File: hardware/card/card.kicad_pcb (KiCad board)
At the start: 4 copper layers, 116 x 106 mm, 0 parts

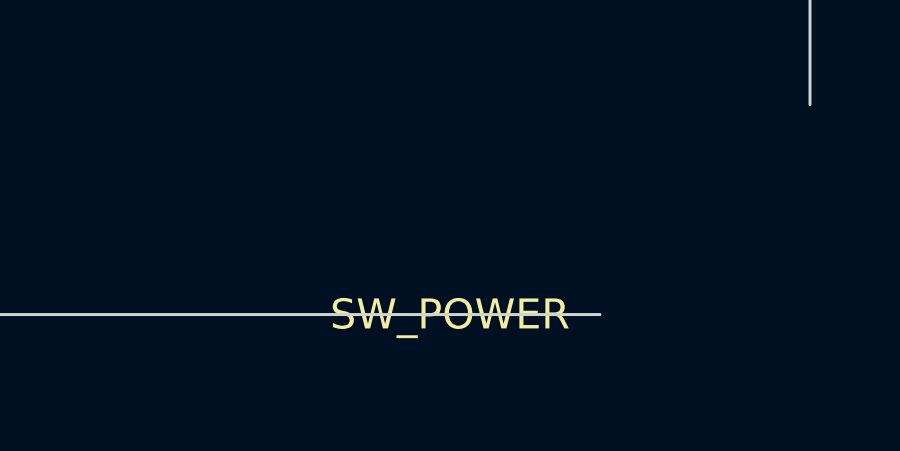
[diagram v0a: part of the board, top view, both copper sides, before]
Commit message: hardware: replace U7 power latch with a slide switch (hard off)
Owner-approved power model: top-edge SPDT slide switch gates the TPS63070
EN pin; hard off is the normal off (Game Boy/Arduboy style, ~1-1.5 s tuned
cold boot, end-of-level atomic saves). Deletes the U7 latch IC and SYSOFF
wiring, frees GPIO8, adds a VBUS-powered charge LED on BQ24075 CHG, and
demotes deep sleep to an optional idle battery-saver. Closes the U7
pre-route gate from the 2026-07-09 PCB review.

Co-authored-by: Cursor <cursoragent@cursor.com>
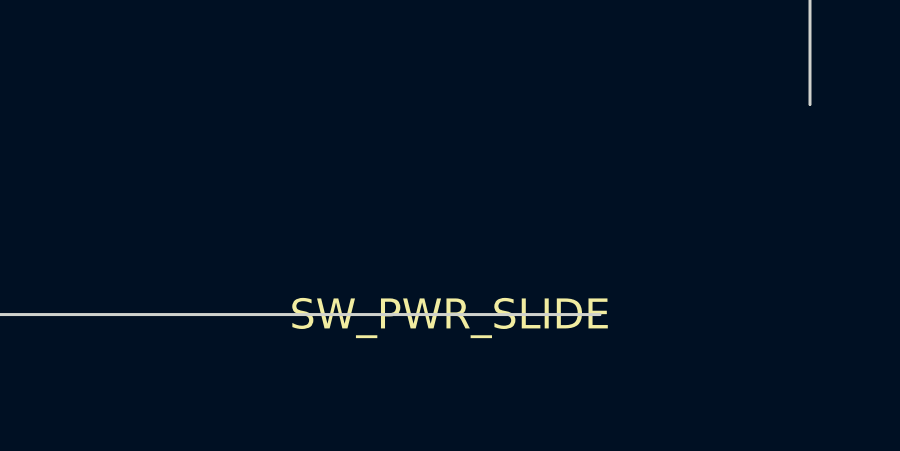
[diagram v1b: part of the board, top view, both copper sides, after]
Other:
- board text added: "SW_PWR_SLIDE"
- board text removed: "SW_POWER"
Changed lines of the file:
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@@
     (effects (font (size 1 1) (thickness 0.15)) (justify center)))
   (gr_circle (center 106 106.5) (end 106.5 106.5) (stroke (width 0.12) (type default)) (fill none) (layer "F.Fab"))
-  (gr_text "SW_POWER" (at 106 108 0) (layer "F.SilkS")
+  (gr_text "SW_PWR_SLIDE" (at 106 108 0) (layer "F.SilkS")
     (effects (font (size 1 1) (thickness 0.15)) (justify center)))
   (gr_circle (center 118.5 92) (end 119 92) (stroke (width 0.12) (type default)) (fill none) (layer "F.Fab"))
@@
   (gr_text "control_band" (at 60 39.5 0) (layer "Cmts.User")
     (effects (font (size 1 1) (thickness 0.12)) (justify center)))
-  (gr_rect (start 8 9) (end 36 37) (stroke (width 0.12) (type dash)) (fill none) (layer "Dwgs.User"))
-  (gr_text "dpad_support" (at 22 38.5 0) (layer "Dwgs.User")
+  (gr_rect (start 18 19) (end 26 27) (stroke (width 0.12) (type dash)) (fill none) (layer "Dwgs.User"))
+  (gr_text "dpad_support" (at 22 28.5 0) (layer "Dwgs.User")
     (effects (font (size 1 1) (thickness 0.12)) (justify center)))
   (gr_rect (start 70 3) (end 100 33) (stroke (width 0.12) (type dash)) (fill none) (layer "Dwgs.User"))

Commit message: hardware: go chip-down ESP32-P4NRW32X, drop WiFi, close display Z-stack
Owner-approved reversal of the module-for-spin-1 decision: the Waveshare
module is 3.3 mm tall, which fails the 9.5 mm display-zone stack (~10.5 mm),
and its C6 radio would ship dark since v1 needs no WiFi. Bare QFN104 chip
(0.9 mm) closes the stack at ~8.2 mm. Adds flash/crystal/DC-DC support
parts to connectivity (copied from the Espressif reference design at
capture), shrinks the back compute keep-out to a 20x20 chip-down cluster,
strips module castellation pin numbers from the pin budget, and records
both Z-stack closure tables in the spec. BOM must use the X silicon
revision (plain NRW32 is EOL).

Co-authored-by: Cursor <cursoragent@cursor.com>
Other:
- board text added: "back_esp32_p4_chip_down"
- board text removed: "back_esp32_p4_module"
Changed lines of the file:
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@@
   (gr_text "back_bat_1s_pouch" (at 60 38.5 0) (layer "Eco2.User")
     (effects (font (size 1 1) (thickness 0.12)) (justify center)))
-  (gr_rect (start 47.5 42) (end 72.5 67) (stroke (width 0.12) (type dash)) (fill none) (layer "Eco2.User"))
-  (gr_text "back_esp32_p4_module" (at 60 68.5 0) (layer "Eco2.User")
+  (gr_rect (start 50 44.5) (end 70 64.5) (stroke (width 0.12) (type dash)) (fill none) (layer "Eco2.User"))
+  (gr_text "back_esp32_p4_chip_down" (at 60 66 0) (layer "Eco2.User")
     (effects (font (size 1 1) (thickness 0.12)) (justify center)))
   (gr_rect (start 76 42) (end 98 53) (stroke (width 0.12) (type dash)) (fill none) (layer "Eco2.User"))

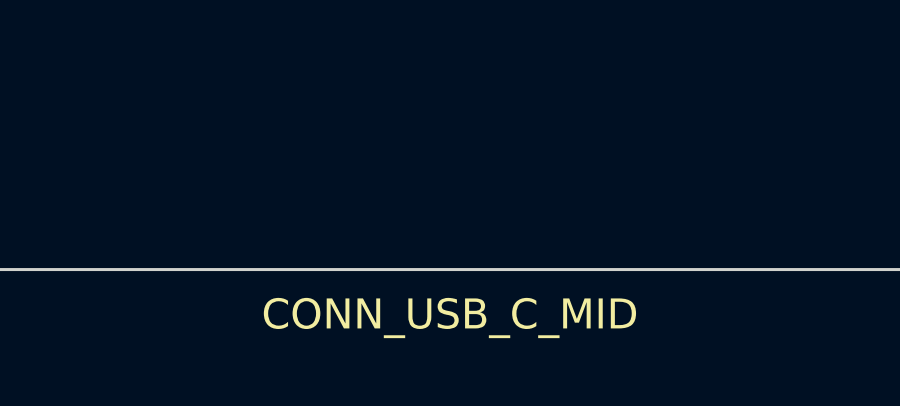
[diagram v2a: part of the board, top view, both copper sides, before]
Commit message: hardware: back-mount the USB-C with a rear-shell bump; lock battery requirements
Owner decisions: J1 becomes a standard 16-pin SMD receptacle (TYPE-C-31-M-12
class, JLC basic part) on the PCB back at the top edge, absorbed by a local
~1 mm rear-shell bump (depthProfile.usbBump). This deletes the mid-mount
board notch and the last display-zone Z-stack interaction. Battery is now
specified by requirements (403048 class <=4.3 mm incl. PCM, built-in
protection, wired leads + JST-SH/PH connector) with the exact SKU deferred
to order-time sample measurement.

Co-authored-by: Cursor <cursoragent@cursor.com>
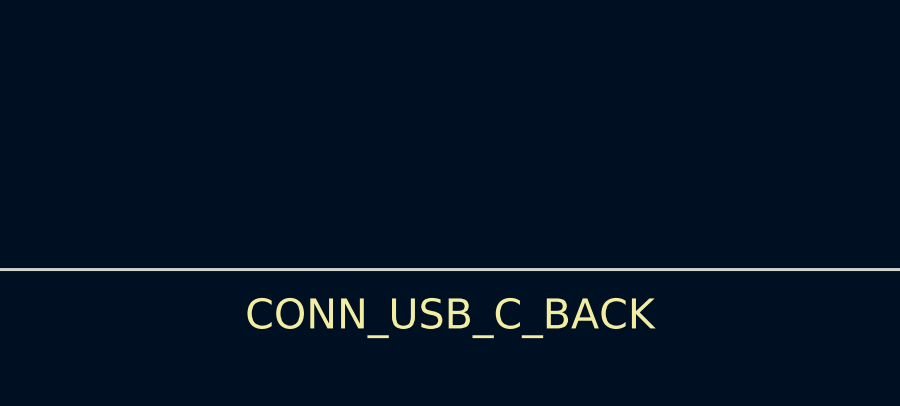
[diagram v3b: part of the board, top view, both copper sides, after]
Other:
- board text added: "CONN_USB_C_BACK"
- board text added: "back_usb_c_back"
- board text removed: "CONN_USB_C_MID"
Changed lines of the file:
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@@
     (effects (font (size 1 1) (thickness 0.15)) (justify center)))
   (gr_circle (center 25 108) (end 25.5 108) (stroke (width 0.12) (type default)) (fill none) (layer "F.Fab"))
-  (gr_text "CONN_USB_C_MID" (at 25 109.5 0) (layer "F.SilkS")
+  (gr_text "CONN_USB_C_BACK" (at 25 109.5 0) (layer "F.SilkS")
     (effects (font (size 1 1) (thickness 0.15)) (justify center)))
   (gr_circle (center 106 106.5) (end 106.5 106.5) (stroke (width 0.12) (type default)) (fill none) (layer "F.Fab"))
@@
   (gr_text "back_pmic_cluster" (at 87 54.5 0) (layer "Eco2.User")
     (effects (font (size 1 1) (thickness 0.12)) (justify center)))
+  (gr_rect (start 18 99) (end 32 108) (stroke (width 0.12) (type dash)) (fill none) (layer "Eco2.User"))
+  (gr_text "back_usb_c_back" (at 25 109.5 0) (layer "Eco2.User")
+    (effects (font (size 1 1) (thickness 0.12)) (justify center)))
 )
